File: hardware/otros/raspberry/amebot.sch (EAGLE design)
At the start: 7 parts, among them IC1 L293DB

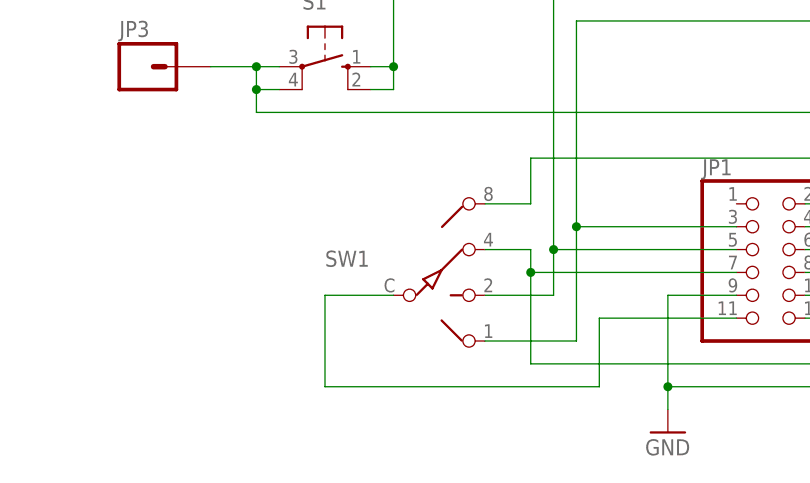
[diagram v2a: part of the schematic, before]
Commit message: 
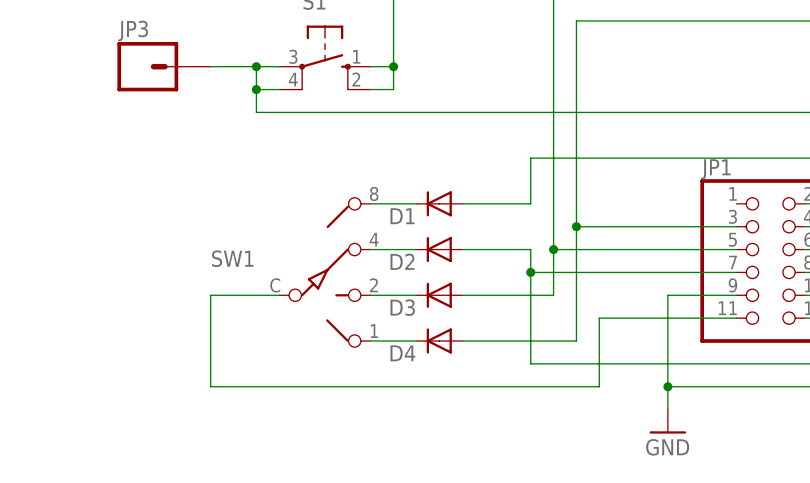
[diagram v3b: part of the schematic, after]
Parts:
- added D1, D2, D3, D4: (no value), diode:DIODE-MICROMELF-W
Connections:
- new net N$1: D1.C, SW1.8
- new net N$15: D2.C, SW1.4
- new net N$16: D3.C, SW1.2
- new net N$17: D4.C, SW1.1
- net N$14: now also D2.A; no longer SW1.4
- net N$3: now also D4.A; no longer SW1.1
- net N$4: now also D3.A; no longer SW1.2
- net N$6: now also D1.A; no longer SW1.8
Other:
- moved on the sheet: SW1
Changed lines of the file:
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@@
 <part name="S1" library="switch-omron" deviceset="10-XX" device=""/>
 <part name="JP2" library="pinhead" deviceset="PINHD-1X5" device=""/>
+<part name="D1" library="diode" deviceset="DIODE-" device="MICROMELF-W"/>
+<part name="D2" library="diode" deviceset="DIODE-" device="MICROMELF-W"/>
+<part name="D3" library="diode" deviceset="DIODE-" device="MICROMELF-W"/>
+<part name="D4" library="diode" deviceset="DIODE-" device="MICROMELF-W"/>
 </parts>
 <sheets>
@@
 <instances>
 <instance part="JP1" gate="A" x="60.96" y="35.56"/>
-<instance part="SW1" gate="A" x="25.4" y="30.48"/>
+<instance part="SW1" gate="A" x="12.7" y="30.48"/>
 <instance part="IC1" gate="G$1" x="124.46" y="68.58"/>
 <instance part="X1" gate="-1" x="-20.32" y="91.44"/>
@@
 <instance part="S1" gate="1" x="12.7" y="55.88" rot="R270"/>
 <instance part="JP2" gate="A" x="101.6" y="35.56"/>
+<instance part="D1" gate="G$1" x="25.4" y="40.64" rot="R180"/>
+<instance part="D2" gate="G$1" x="25.4" y="35.56" rot="R180"/>
+<instance part="D3" gate="G$1" x="25.4" y="30.48" rot="R180"/>
+<instance part="D4" gate="G$1" x="25.4" y="25.4" rot="R180"/>
 </instances>
 <busses>
@@
 <junction x="40.64" y="38.1"/>
 <wire x1="40.64" y1="38.1" x2="40.64" y2="25.4" width="0.1524" layer="91"/>
-<pinref part="SW1" gate="A" pin="1"/>
-<wire x1="40.64" y1="25.4" x2="30.48" y2="25.4" width="0.1524" layer="91"/>
+<wire x1="40.64" y1="25.4" x2="27.94" y2="25.4" width="0.1524" layer="91"/>
+<pinref part="D4" gate="G$1" pin="A"/>
 </segment>
 </net>
@@
 <wire x1="38.1" y1="35.56" x2="58.42" y2="35.56" width="0.1524" layer="91"/>
 <wire x1="38.1" y1="76.2" x2="38.1" y2="35.56" width="0.1524" layer="91"/>
-<pinref part="SW1" gate="A" pin="2"/>
-<wire x1="30.48" y1="30.48" x2="38.1" y2="30.48" width="0.1524" layer="91"/>
 <wire x1="38.1" y1="30.48" x2="38.1" y2="35.56" width="0.1524" layer="91"/>
 <junction x="38.1" y="35.56"/>
+<wire x1="38.1" y1="30.48" x2="27.94" y2="30.48" width="0.1524" layer="91"/>
+<pinref part="D3" gate="G$1" pin="A"/>
 </segment>
 </net>
@@
 <segment>
 <pinref part="SW1" gate="A" pin="C"/>
-<wire x1="20.32" y1="30.48" x2="12.7" y2="30.48" width="0.1524" layer="91"/>
-<wire x1="12.7" y1="30.48" x2="12.7" y2="20.32" width="0.1524" layer="91"/>
-<wire x1="12.7" y1="20.32" x2="43.18" y2="20.32" width="0.1524" layer="91"/>
+<wire x1="7.62" y1="30.48" x2="0" y2="30.48" width="0.1524" layer="91"/>
+<wire x1="0" y1="30.48" x2="0" y2="20.32" width="0.1524" layer="91"/>
+<wire x1="0" y1="20.32" x2="43.18" y2="20.32" width="0.1524" layer="91"/>
 <wire x1="43.18" y1="20.32" x2="43.18" y2="27.94" width="0.1524" layer="91"/>
 <pinref part="JP1" gate="A" pin="11"/>
@@
 <wire x1="78.74" y1="45.72" x2="35.56" y2="45.72" width="0.1524" layer="91"/>
 <wire x1="35.56" y1="45.72" x2="35.56" y2="40.64" width="0.1524" layer="91"/>
-<pinref part="SW1" gate="A" pin="8"/>
-<wire x1="30.48" y1="40.64" x2="35.56" y2="40.64" width="0.1524" layer="91"/>
 <wire x1="78.74" y1="45.72" x2="78.74" y2="27.94" width="0.1524" layer="91"/>
 <junction x="78.74" y="45.72"/>
 <pinref part="JP1" gate="A" pin="12"/>
 <wire x1="78.74" y1="27.94" x2="66.04" y2="27.94" width="0.1524" layer="91"/>
+<wire x1="35.56" y1="40.64" x2="27.94" y2="40.64" width="0.1524" layer="91"/>
+<pinref part="D1" gate="G$1" pin="A"/>
 </segment>
 </net>
@@
 <net name="N$14" class="0">
 <segment>
-<pinref part="SW1" gate="A" pin="4"/>
-<wire x1="30.48" y1="35.56" x2="35.56" y2="35.56" width="0.1524" layer="91"/>
 <wire x1="35.56" y1="35.56" x2="35.56" y2="33.02" width="0.1524" layer="91"/>
 <pinref part="IC1" gate="G$1" pin="3Y"/>
@@
 <wire x1="35.56" y1="33.02" x2="35.56" y2="22.86" width="0.1524" layer="91"/>
 <junction x="35.56" y="33.02"/>
-</segment>
-</net>
+<wire x1="35.56" y1="35.56" x2="27.94" y2="35.56" width="0.1524" layer="91"/>
+<pinref part="D2" gate="G$1" pin="A"/>
+</segment>
+</net>
+<net name="N$1" class="0">
+<segment>
+<pinref part="SW1" gate="A" pin="8"/>
+<wire x1="22.86" y1="40.64" x2="17.78" y2="40.64" width="0.1524" layer="91"/>
+<pinref part="D1" gate="G$1" pin="C"/>
+</segment>
+</net>
+<net name="N$15" class="0">
+<segment>
+<pinref part="SW1" gate="A" pin="4"/>
+<wire x1="22.86" y1="35.56" x2="17.78" y2="35.56" width="0.1524" layer="91"/>
+<pinref part="D2" gate="G$1" pin="C"/>
+</segment>
+</net>
+<net name="N$16" class="0">
+<segment>
+<pinref part="SW1" gate="A" pin="2"/>
+<wire x1="22.86" y1="30.48" x2="17.78" y2="30.48" width="0.1524" layer="91"/>
+<pinref part="D3" gate="G$1" pin="C"/>
+</segment>
+</net>
+<net name="N$17" class="0">
+<segment>
+<pinref part="SW1" gate="A" pin="1"/>
+<wire x1="22.86" y1="25.4" x2="17.78" y2="25.4" width="0.1524" layer="91"/>
+<pinref part="D4" gate="G$1" pin="C"/>
+</segment>
+</net>
